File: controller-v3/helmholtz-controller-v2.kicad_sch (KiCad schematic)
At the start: 60 parts, among them J1 Screw_Terminal_01x02, J2 Screw_Terminal_01x02, J3 Screw_Terminal_01x02, J4 Screw_Terminal_01x02, J5 Conn_01x04, U1 BDS63150AFM, U2 BDS63150AFM, U3 INA226, U4 INA226, U5 BDS63150AFM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

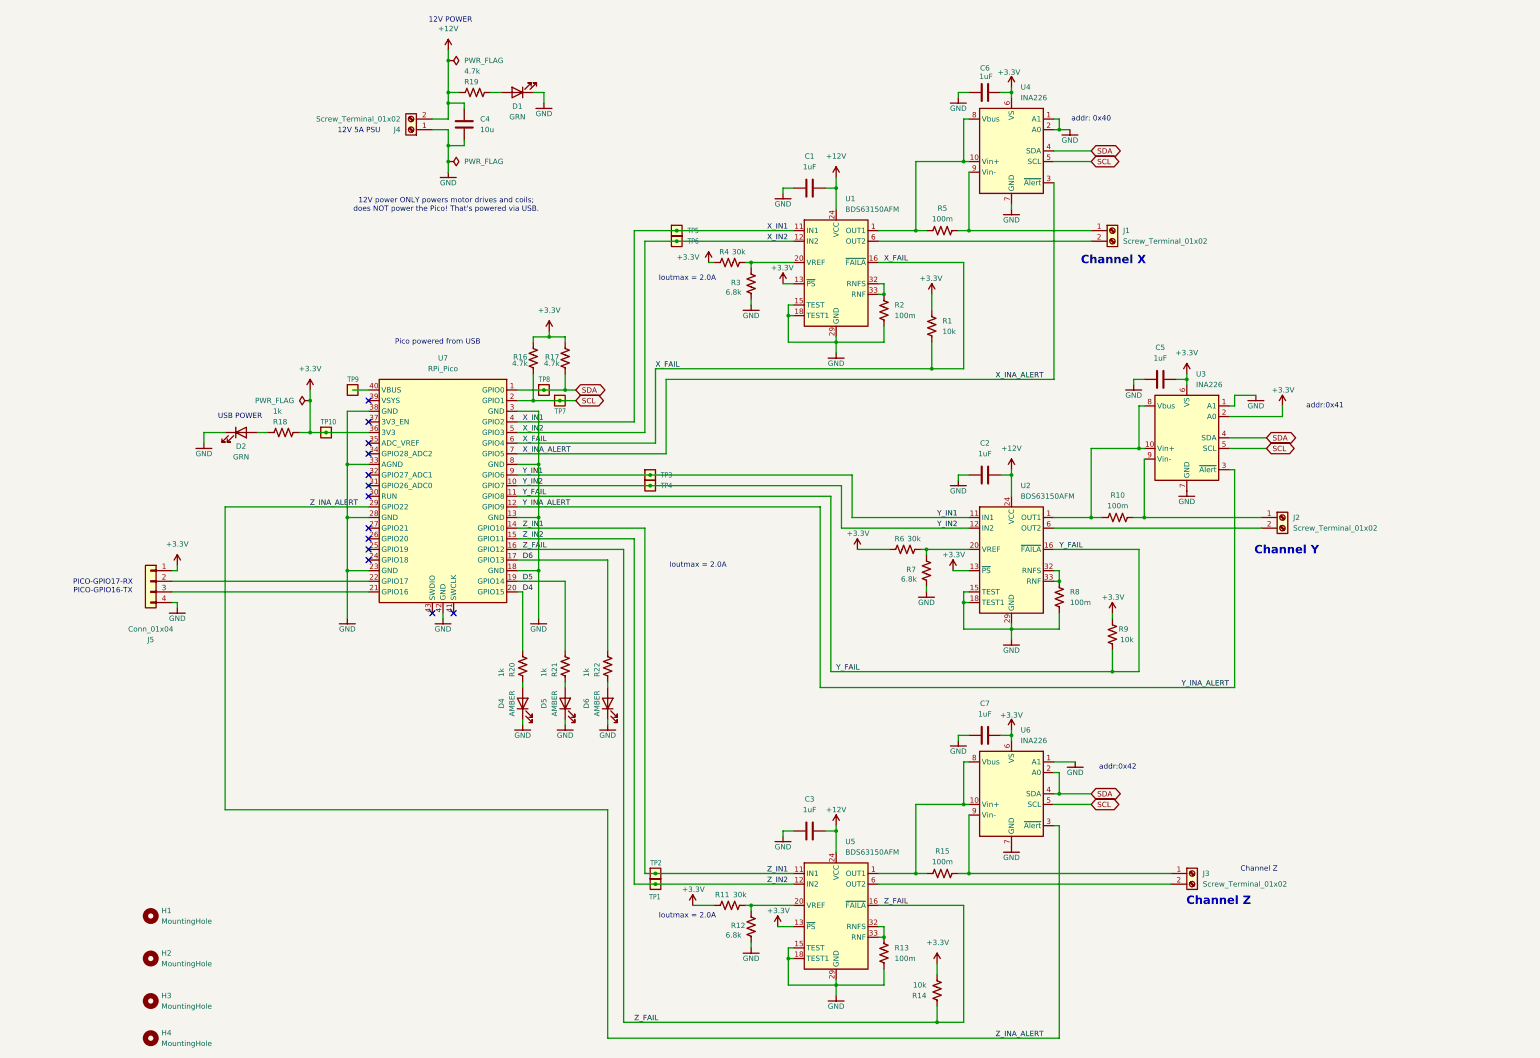
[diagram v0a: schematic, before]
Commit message: Update to schematic
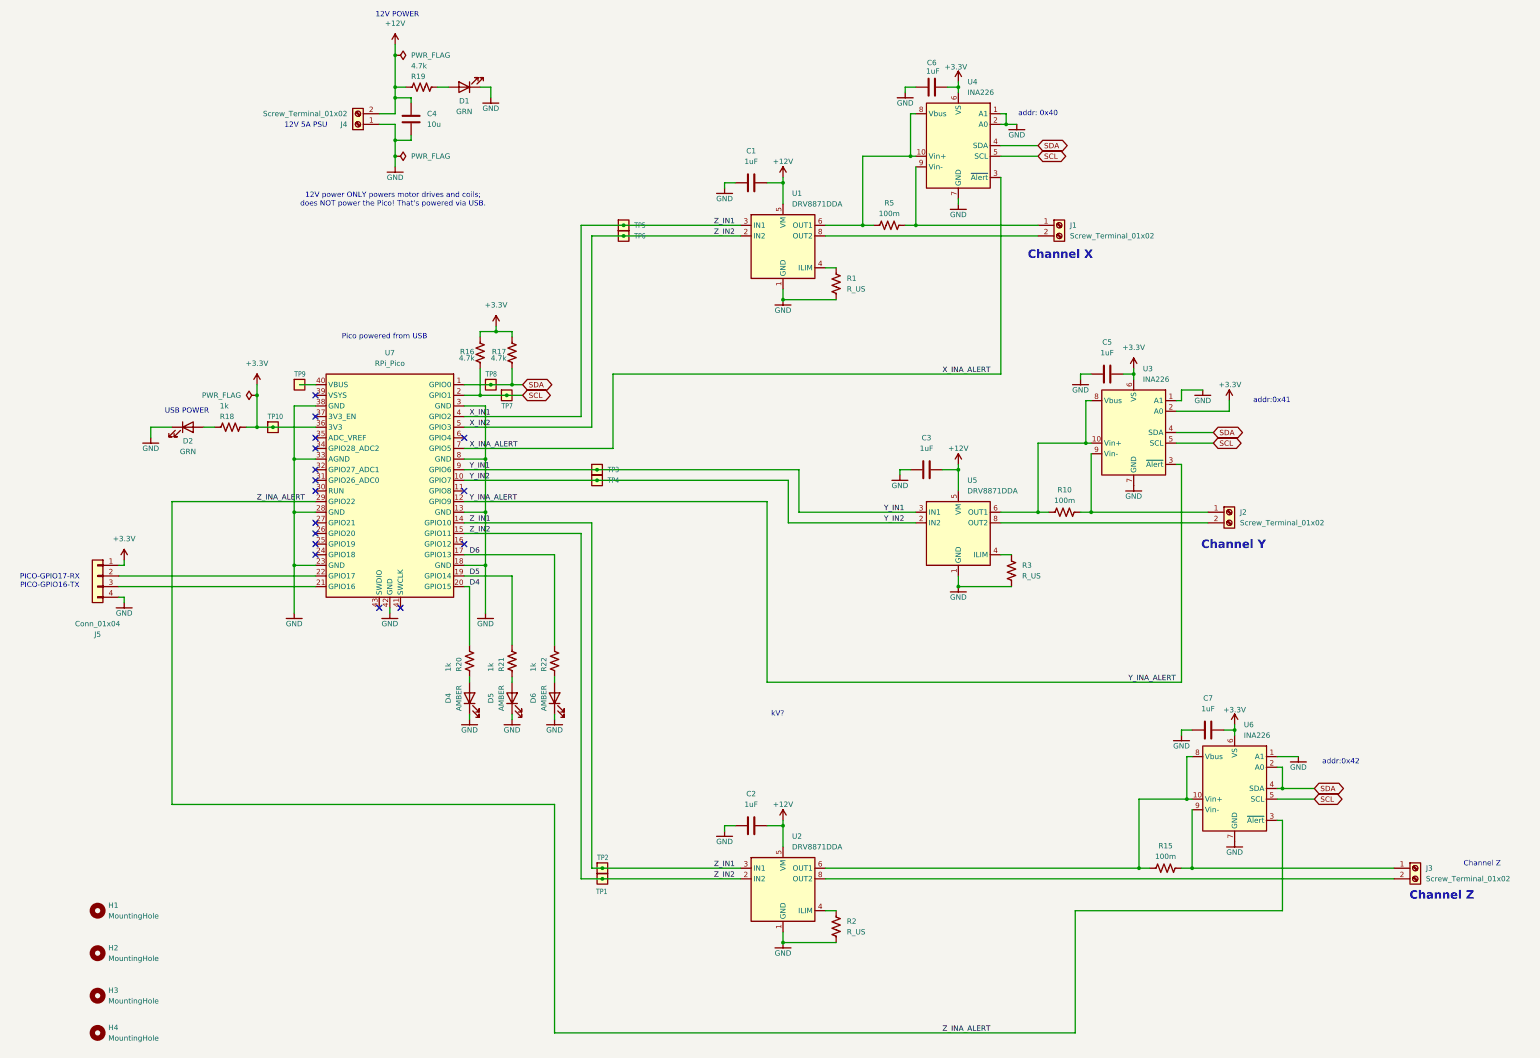
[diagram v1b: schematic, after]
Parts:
- removed R11, R4, R6: 30k, Resistor_SMD:R_0603_1608Metric, symbol Device:R_US
- removed R12, R7: 6.8k, Resistor_SMD:R_0603_1608Metric, symbol Device:R_US
- removed R13, R8: 100m, Resistor_SMD:R_1206_3216Metric, symbol Device:R_US
- removed R14, R9: 10k, Resistor_SMD:R_0603_1608Metric, symbol Device:R_US
- removed U1, U2, U5: BDS63150AFM, psas-footprints:U-BD63150AFM, symbol U-Rohm-BD63150AFM-E2-h-bridge-motor-driver:BDS63150AFM-E2
- added U1, U2, U5: DRV8871DDA, Package_SO:Texas_HTSOP-8-1EP_3.9x4.9mm_P1.27mm_EP2.95x4.9mm_Mask2.4x3.1mm_ThermalVias, symbol Driver_Motor:DRV8871DDA
- R1: value 10k -> R_US; DIS Digikey -> (none); DPN RMCF0603FT10K0CT-ND -> (none); MFR Stackpole Electronics Inc -> (none); MPN RMCF0603FT10K0 -> (none)
- R2: value 100m -> R_US; footprint Resistor_SMD:R_1206_3216Metric -> Resistor_SMD:R_0603_1608Metric; DIS Digikey -> (none); DPN CSR1206FTR100CT-ND -> (none); MFR Stackpole Electronics Inc -> (none); MPN CSR1206FTR100 -> (none)
- R3: value 6.8k -> R_US; DIS Digikey -> (none); DPN 311-6.8KGRCT-ND -> (none); MFR YAGEO -> (none); MPN RC0603JR-076K8L -> (none)
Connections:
- net Z_IN1 is gone; now on net X_IN1: TP2.1, U7.14 (GPIO10)
- net Z_IN2 is gone; now on net X_IN2: TP1.1, U7.15 (GPIO11)
- net +12V: now also U1.5 (VM), U2.5 (VM), U5.5 (VM)
- net +3.3V: no longer R1.1
- net GND: now also R1.2, R3.2, U1.1 (GND), U1.7 (GND), U1.9 (GND), U2.1 (GND), U2.7 (GND), U2.9 (GND), U5.1 (GND), U5.7 (GND), U5.9 (GND); no longer R3.1
- net X_IN1: now also U1.3 (IN1), U2.3 (IN1)
- net X_IN2: now also U1.2 (IN2), U2.2 (IN2)
- net Y_IN1: now also U5.3 (IN1)
- net Y_IN2: now also U5.2 (IN2)
- net at R10.1, U3.10 (Vin+), U3.8 (Vbus): now also U5.6 (OUT1)
- net at J2.2 (Pin_2): now also U5.8 (OUT2)
- net at R15.1, U6.10 (Vin+), U6.8 (Vbus): now also U2.6 (OUT1)
- net at J3.2 (Pin_2): now also U2.8 (OUT2)
- net at J1.2 (Pin_2): now also U1.8 (OUT2)
- net at R2.1: now also U2.4 (ILIM)
- net at R5.1, U4.10 (Vin+), U4.8 (Vbus): now also U1.6 (OUT1)
- net X_FAIL: no longer names the net of U7.6 (GPIO4)
- net X_FAIL: no longer R1.2
- net Y_FAIL: no longer names the net of U7.11 (GPIO8)
- net Z_FAIL: no longer names the net of U7.16 (GPIO12)
- new net: R3.1, U5.4 (ILIM)
- new net: R1.1, U1.4 (ILIM)
- no-connect marks 13 -> 16
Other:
- note added: "kV?"
- note removed: "Ioutmax = 2.0A"
- moved on the sheet: C4, C5, C6, C7, D1, D2, D4, D5, D6, H1, H2, H3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

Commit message: Board mostly laid out
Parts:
- added R11, R4, R6, R7, R8, R9: R_US, Resistor_SMD:R_0603_1608Metric, symbol Device:R_US
- D1, D2, D4, D5, D6: symbol Device:LED -> Device:LED_Small_Filled
- J1, J2, J3: footprint TerminalBlock_Phoenix:TerminalBlock_Phoenix_PT-1,5-2-3.5-H_1x02_P3.50mm_Horizontal -> Connector_AMASS:AMASS_XT30PW-F_1x02_P2.50mm_Horizontal
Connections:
- net +3.3V: no longer J5.1 (Pin_1)
- net GND: now also R11.2, R4.2, R6.2, R7.2, R8.2, R9.2
- net X_IN1: now also R7.1; no longer TP2.1, U2.3 (IN1), U7.14 (GPIO10)
- net X_IN2: now also R4.1; no longer TP1.1, U2.2 (IN2), U7.15 (GPIO11)
- net Y_IN1: now also R11.1
- net Y_IN2: now also R9.1
- net Z_INA_ALERT: now also U7.16 (GPIO12); no longer U7.29 (GPIO22)
- net at U5.8 (OUT2): now also J2.1 (Pin_1); no longer J2.2 (Pin_2)
- net at R10.2, U3.9 (Vin-): now also J2.2 (Pin_2); no longer J2.1 (Pin_1)
- net at U2.8 (OUT2): now also J3.1 (Pin_1); no longer J3.2 (Pin_2)
- net at R5.2, U4.9 (Vin-): now also J1.2 (Pin_2); no longer J1.1 (Pin_1)
- net at U1.8 (OUT2): now also J1.1 (Pin_1); no longer J1.2 (Pin_2)
- net at R15.2, U6.9 (Vin-): now also J3.2 (Pin_2); no longer J3.1 (Pin_1)
- net D6: no longer names the net of R22.2, U7.17 (GPIO13)
- new net Z_IN1: R8.1, TP2.1, U2.3 (IN1), U7.14 (GPIO10)
- new net Z_IN2: R6.1, TP1.1, U2.2 (IN2), U7.15 (GPIO11)
- no-connect marks 16 -> 17
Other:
- moved on the sheet: R15

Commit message: Done!
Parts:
- C1, C2, C3, C5, C6, C7: DPN 1276-1066-1-ND -> 490-10675-2-ND; MFR Samsung Electro-Mechanics -> Murata Electronics; MPN CL21B105KAFNNNE -> GCM21BR71H105KA03L
- C4: DIS Digikey -> DigiKey; DPN 1276-2891-1-ND -> 490-GRT21BC71E106KE13KCT-ND; MFR Samsung Electro-Mechanics -> Murata Electronics; MPN CL21A106KAYNNNE -> GRT21BC71E106KE13K
- D1, D2: DIS Digikey -> DigiKey; DPN 1830-1062-1-ND -> 732-4971-1-ND; MFR Inolux -> Wurth; MPN IN-S63AT5G -> 150060GS75000
- D4, D5, D6: DIS Digikey -> DigiKey; DPN 1830-1064-1-ND -> 732-150060AS75000CT-ND; MFR Inolux -> Wurth; MPN IN-S63AT5A -> 150060AS75000
- J1, J2, J3: DIS Digikey -> Amazon; DPN 277-5719-ND -> https://www.amazon.com/5Pairs-XT30PW-Connector-Horizontal-X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; MFR Phoenix Contact -> Amass; MPN 1751248 -> (none)
- R1, R2, R3: value R_US -> 32k; DIS (none) -> DigiKey; DPN (none) -> 738-RNCF0603BTE32K0TR-ND; MFR (none) -> Stackpole Electronics; MPN (none) -> RNCF0603BTE32K0
- R11, R4, R6, R7, R8, R9: value R_US -> 10k; DIS (none) -> DigiKey; DPN (none) -> RMCF0603FT10K0CT-ND; MFR (none) -> Stackpole Electronics; MPN (none) -> RMCF0603FT10K0
- U1, U2, U5: DIS (none) -> DigiKey; DPN (none) -> 296-44509-5-ND; MFR (none) -> Texas Instruments; MPN (none) -> DRV8871DDA
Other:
- note removed: "kV?"

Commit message: Some polish
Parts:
- J1, J2, J3, J4: symbol Connector:Screw_Terminal_01x02 -> Connector_Generic:Conn_01x02
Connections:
- net D4: no longer names the net of R20.2, U7.20 (GPIO15)
- net D5: no longer names the net of R21.2, U7.19 (GPIO14)
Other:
- note added: "32 k = 2.0 A max"
- moved on the sheet: C7, R15, U6

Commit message: Requested changes
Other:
- moved on the sheet: J1, J3
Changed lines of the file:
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@@
 	(text "Channel Z"
 		(exclude_from_sim no)
-		(at 322.072 226.822 0)
+		(at 266.192 226.822 0)
 		(effects
 			(font
@@
 	(wire
 		(pts
-			(xy 242.57 66.04) (xy 297.18 66.04)
-		)
-		(stroke
-			(width 0)
-			(type default)
-		)
-	)
-	(wire
-		(pts
 			(xy 120.65 36.83) (xy 120.65 35.56)
 		)
@@
 	(wire
 		(pts
-			(xy 283.21 138.43) (xy 311.15 138.43)
-		)
-		(stroke
-			(width 0)
-			(type default)
-		)
-	)
-	(wire
-		(pts
 			(xy 83.82 104.14) (xy 83.82 114.3)
 		)
@@
 	(wire
 		(pts
-			(xy 219.71 222.25) (xy 317.5 222.25)
+			(xy 219.71 222.25) (xy 261.62 222.25)
 		)
 		(stroke
@@
 	(wire
 		(pts
-			(xy 261.62 137.16) (xy 284.48 137.16)
+			(xy 261.62 137.16) (xy 311.15 137.16)
 		)
 		(stroke
@@
 	(wire
 		(pts
-			(xy 219.71 68.58) (xy 242.57 68.58)
+			(xy 219.71 68.58) (xy 262.89 68.58)
 		)
 		(stroke
@@
 	(wire
 		(pts
-			(xy 297.18 69.85) (xy 297.18 68.58)
-		)
-		(stroke
-			(width 0)
-			(type default)
-		)
-	)
-	(wire
-		(pts
 			(xy 92.71 158.75) (xy 92.71 147.32)
 		)
@@
 	(wire
 		(pts
-			(xy 284.48 137.16) (xy 284.48 134.62)
-		)
-		(stroke
-			(width 0)
-			(type default)
-		)
-	)
-	(wire
-		(pts
 			(xy 133.35 132.08) (xy 208.28 132.08)
 		)
@@
 	(wire
 		(pts
-			(xy 317.5 219.71) (xy 245.11 219.71)
+			(xy 261.62 219.71) (xy 245.11 219.71)
 		)
 		(stroke
@@
 	(wire
 		(pts
-			(xy 284.48 134.62) (xy 311.15 134.62)
+			(xy 251.46 33.02) (xy 251.46 34.29)
 		)
 		(stroke
@@
 	(wire
 		(pts
-			(xy 251.46 33.02) (xy 251.46 34.29)
+			(xy 270.51 134.62) (xy 273.05 134.62)
 		)
 		(stroke
@@
 	(wire
 		(pts
-			(xy 270.51 134.62) (xy 273.05 134.62)
+			(xy 243.84 193.04) (xy 243.84 203.2)
 		)
 		(stroke
@@
 	(wire
 		(pts
-			(xy 243.84 193.04) (xy 243.84 203.2)
+			(xy 219.71 66.04) (xy 228.6 66.04)
 		)
 		(stroke
@@
 	(wire
 		(pts
-			(xy 219.71 66.04) (xy 228.6 66.04)
+			(xy 116.84 41.91) (xy 116.84 45.72)
 		)
 		(stroke
@@
 	(wire
 		(pts
-			(xy 116.84 41.91) (xy 116.84 45.72)
+			(xy 116.84 33.02) (xy 116.84 35.56)
 		)
 		(stroke
@@
 	(wire
 		(pts
-			(xy 116.84 33.02) (xy 116.84 35.56)
+			(xy 283.21 134.62) (xy 311.15 134.62)
 		)
 		(stroke
@@
 	(wire
 		(pts
-			(xy 311.15 138.43) (xy 311.15 137.16)
-		)
-		(stroke
-			(width 0)
-			(type default)
-		)
-	)
-	(wire
-		(pts
 			(xy 210.82 137.16) (xy 224.79 137.16)
 		)
@@
 	(wire
 		(pts
-			(xy 241.3 69.85) (xy 297.18 69.85)
+			(xy 241.3 66.04) (xy 262.89 66.04)
 		)
 		(stroke
@@
 	(wire
 		(pts
-			(xy 242.57 68.58) (xy 242.57 66.04)
-		)
-		(stroke
-			(width 0)
-			(type default)
-		)
-	)
-	(wire
-		(pts
 			(xy 133.35 111.76) (xy 161.29 111.76)
 		)
@@
 	(wire
 		(pts
-			(xy 283.21 134.62) (xy 283.21 138.43)
-		)
-		(stroke
-			(width 0)
-			(type default)
-		)
-	)
-	(wire
-		(pts
 			(xy 154.94 144.78) (xy 154.94 166.37)
 		)
@@
 	(wire
 		(pts
-			(xy 241.3 66.04) (xy 241.3 69.85)
-		)
-		(stroke
-			(width 0)
-			(type default)
-		)
-	)
-	(wire
-		(pts
 			(xy 133.35 144.78) (xy 154.94 144.78)
 		)
@@
 	(symbol
 		(lib_id "Connector_Generic:Conn_01x02")
-		(at 322.58 222.25 0)
+		(at 266.7 222.25 0)
 		(mirror x)
 		(unit 1)
@@
 		(dnp no)
 		(property "Reference" "J3"
-			(at 325.12 222.2501 0)
+			(at 269.24 222.2501 0)
 			(effects
 				(font
@@
 		)
 		(property "Value" "Screw_Terminal_01x02"
-			(at 325.12 219.7101 0)
+			(at 269.24 219.7101 0)
 			(effects
 				(font
@@
 		)
 		(property "Footprint" "Connector_AMASS:AMASS_XT30PW-F_1x02_P2.50mm_Horizontal"
-			(at 322.58 222.25 0)
+			(at 266.7 222.25 0)
 			(effects
 				(font
@@
 		)
 		(property "Datasheet" "~"
-			(at 322.58 222.25 0)
+			(at 266.7 222.25 0)
 			(effects
 				(font
@@
 		)
 		(property "Description" "Generic connector, single row, 01x02, script generated (kicad-library-utils/schlib/autogen/connector/)"
-			(at 322.58 222.25 0)
+			(at 266.7 222.25 0)
 			(effects
 				(font
@@
 		)
 		(property "DIS" "Amazon"
-			(at 322.58 222.25 0)
+			(at 266.7 222.25 0)
 			(effects
 				(font
@@
 		)
 		(property "DPN" "https://www.amazon.com/5Pairs-XT30PW-Connector-Horizontal-XT30PW-M/dp/B0D1QTFGBV/ref=sr_1_12?crid=1UGZHPKL4Z6FO&sprefix=xt30pw%2Caps%2C180&sr=8-12&th=1"
-			(at 322.58 222.25 0)
+			(at 266.7 222.25 0)
 			(effects
 				(font
@@
 		)
 		(property "MFR" "Amass"
-			(at 322.58 222.25 0)
+			(at 266.7 222.25 0)
 			(effects
 				(font
@@
 		)
 		(property "MPN" ""
-			(at 322.58 222.25 0)
+			(at 266.7 222.25 0)
 			(effects
 				(font
@@
 	(symbol
 		(lib_id "Connector_Generic:Conn_01x02")
-		(at 302.26 66.04 0)
+		(at 267.97 68.58 0)
+		(mirror x)
 		(unit 1)
 		(exclude_from_sim no)
@@
 		(on_board yes)
 		(dnp no)
-		(fields_autoplaced yes)
 		(property "Reference" "J1"
-			(at 304.8 66.0399 0)
+			(at 270.51 68.5801 0)
 			(effects
 				(font
@@
 		)
 		(property "Value" "Screw_Terminal_01x02"
-			(at 304.8 68.5799 0)
+			(at 270.51 66.0401 0)
 			(effects
 				(font
@@
 		)
 		(property "Footprint" "Connector_AMASS:AMASS_XT30PW-F_1x02_P2.50mm_Horizontal"
-			(at 302.26 66.04 0)
+			(at 267.97 68.58 0)
 			(effects
 				(font
@@
 		)
 		(property "Datasheet" "~"
-			(at 302.26 66.04 0)
+			(at 267.97 68.58 0)
 			(effects
 				(font
@@
 		)
 		(property "Description" "Generic connector, single row, 01x02, script generated (kicad-library-utils/schlib/autogen/connector/)"
-			(at 302.26 66.04 0)
+			(at 267.97 68.58 0)
 			(effects
 				(font
@@
 		)
 		(property "DIS" "Amazon"
-			(at 302.26 66.04 0)
+			(at 267.97 68.58 0)
 			(effects
 				(font
@@
 		)
 		(property "DPN" "https://www.amazon.com/5Pairs-XT30PW-Connector-Horizontal-XT30PW-M/dp/B0D1QTFGBV/ref=sr_1_12?crid=1UGZHPKL4Z6FO&sprefix=xt30pw%2Caps%2C180&sr=8-12&th=1"
-			(at 302.26 66.04 0)
+			(at 267.97 68.58 0)
 			(effects
 				(font
@@
 		)
 		(property "MFR" "Amass"
-			(at 302.26 66.04 0)
+			(at 267.97 68.58 0)
 			(effects
 				(font
@@
 		)
 		(property "MPN" ""
-			(at 302.26 66.04 0)
+			(at 267.97 68.58 0)
 			(effects
 				(font
@@
 	(symbol
 		(lib_id "Connector_Generic:Conn_01x02")
-		(at 316.23 134.62 0)
+		(at 316.23 137.16 0)
+		(mirror x)
 		(unit 1)
 		(exclude_from_sim no)
@@
 		(dnp no)
 		(property "Reference" "J2"
-			(at 318.77 134.6199 0)
+			(at 318.77 137.1601 0)
 			(effects
 				(font
@@
 		)
 		(property "Value" "Screw_Terminal_01x02"
-			(at 318.77 137.1599 0)
+			(at 318.77 134.6201 0)
 			(effects
 				(font
@@
 		)
 		(property "Footprint" "Connector_AMASS:AMASS_XT30PW-F_1x02_P2.50mm_Horizontal"
-			(at 316.23 134.62 0)
+			(at 316.23 137.16 0)
 			(effects
 				(font
@@
 		)
 		(property "Datasheet" "~"
-			(at 316.23 134.62 0)
+			(at 316.23 137.16 0)
 			(effects
 				(font
@@
 		)
 		(property "Description" "Generic connector, single row, 01x02, script generated (kicad-library-utils/schlib/autogen/connector/)"
-			(at 316.23 134.62 0)
+			(at 316.23 137.16 0)
 			(effects
 				(font
@@
 		)
 		(property "DIS" "Amazon"
-			(at 316.23 134.62 0)
+			(at 316.23 137.16 0)
 			(effects
 				(font
@@
 		)
 		(property "DPN" "https://www.amazon.com/5Pairs-XT30PW-Connector-Horizontal-XT30PW-M/dp/B0D1QTFGBV/ref=sr_1_12?crid=1UGZHPKL4Z6FO&sprefix=xt30pw%2Caps%2C180&sr=8-12&th=1"
-			(at 316.23 134.62 0)
+			(at 316.23 137.16 0)
 			(effects
 				(font
@@
 		)
 		(property "MFR" "Amass"
-			(at 316.23 134.62 0)
+			(at 316.23 137.16 0)
 			(effects
 				(font
@@
 		)
 		(property "MPN" ""
-			(at 316.23 134.62 0)
+			(at 316.23 137.16 0)
 			(effects
 				(font
